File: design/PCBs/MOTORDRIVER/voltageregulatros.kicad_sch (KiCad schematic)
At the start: 15 parts, among them IC2 LD1117S33CTR, IC3 MC34063ECD-TR, IC4 BQ24133RGYR, IC5 REF3450TIDBVR

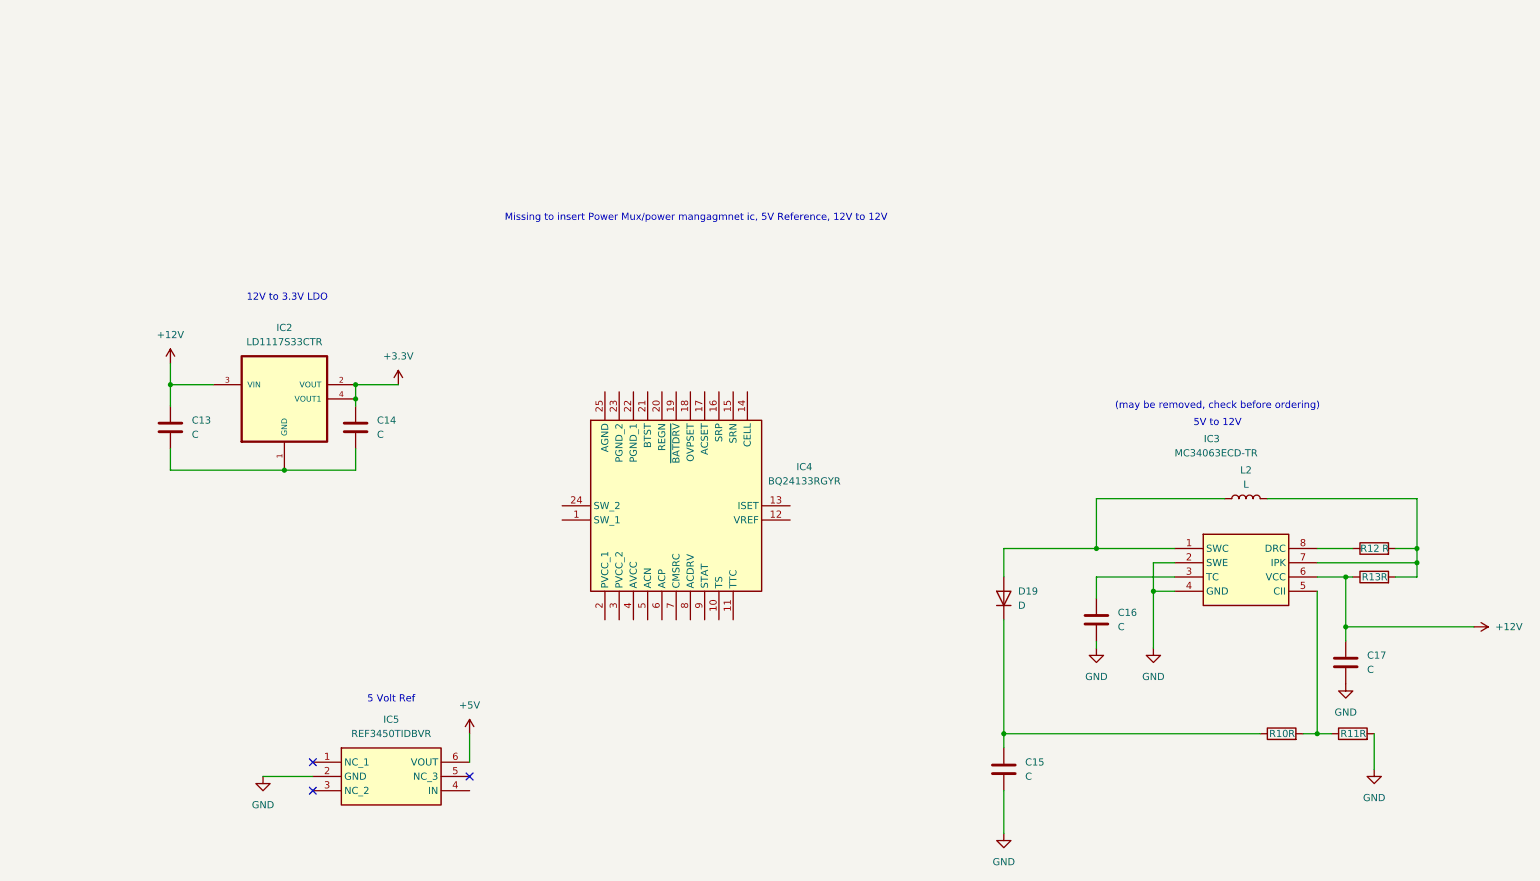
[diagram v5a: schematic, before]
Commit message: Clearer file names for datasheets indicating what kind of component they are. Started on connecting the battery charger Added mosfet ICs for driver gates
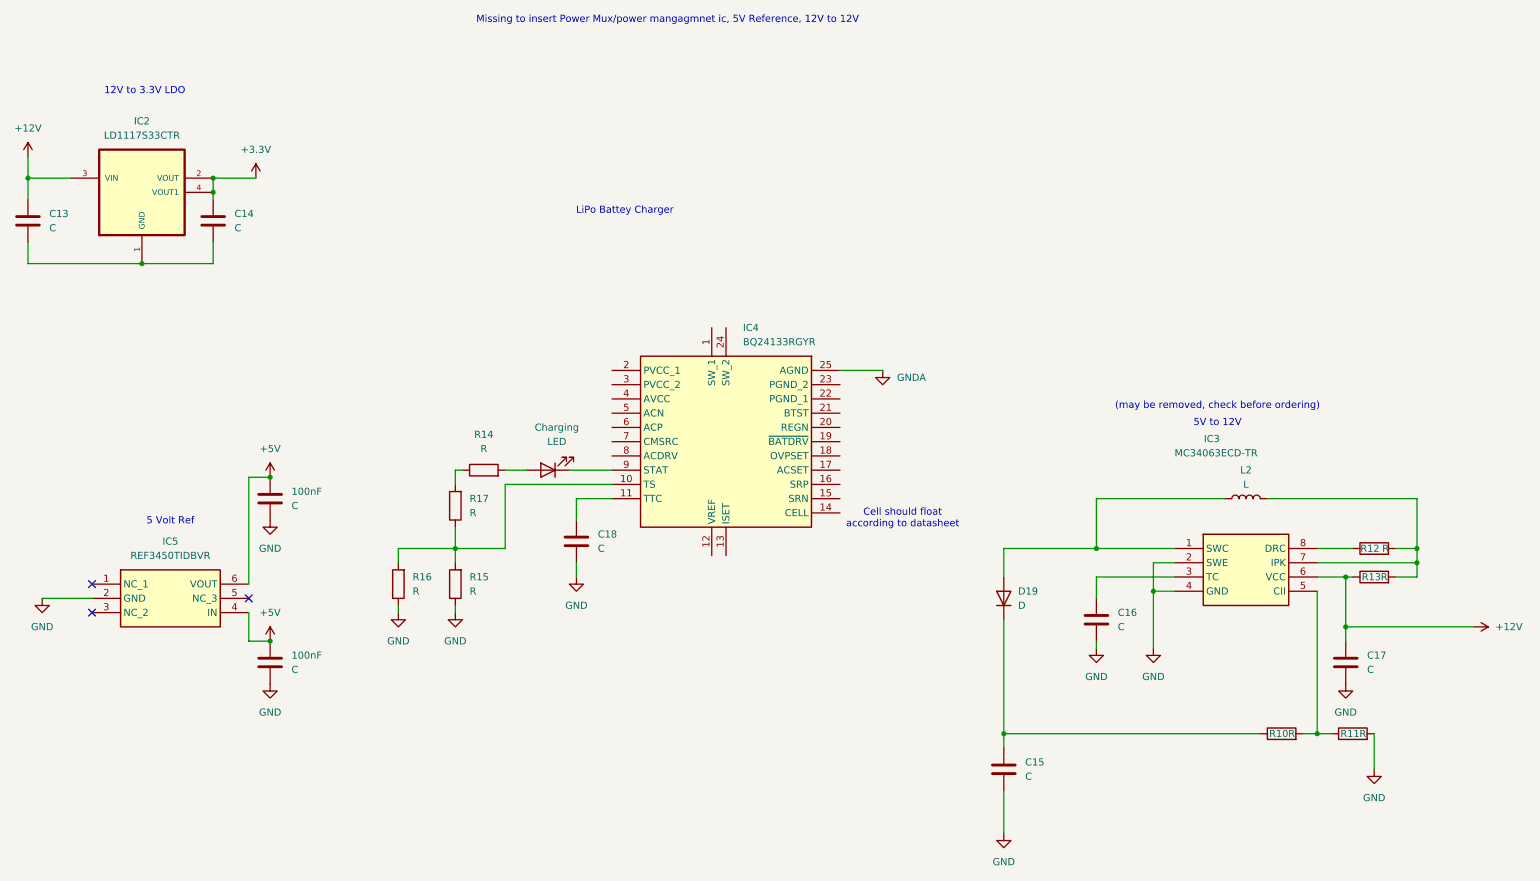
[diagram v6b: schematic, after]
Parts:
- added 100nF (x2), C18: C, symbol Device:C
- added Charging: LED, symbol Device:LED
- added R14, R15, R16, R17: R, symbol Device:R
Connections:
- net +5V: now also IC5.4 (IN), 100nF.1, 100nF.1
- net GND: now also 100nF.2, 100nF.2, C18.2, R15.1, R16.1
- net at IC4.10 (TS): now also R15.2, R16.2, R17.1
- net at IC4.11 (TTC): now also C18.1
- net GNDA: now reaches IC4.25 (AGND)
- net at IC4.9 (STAT): now also Charging.1 (K)
- new net: R14.1, R17.2
- new net: Charging.2 (A), R14.2
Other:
- note added: "Cell should float according to datasheet"
- note added: "LiPo Battey Charger"
- moved on the sheet: C13, C14, IC2, IC4, IC5

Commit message: fixed schematic layout and added shunt resistor and zener diodes for motor stage
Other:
- note added: "12V out"
- note removed: "(may be removed, check before ordering)"
- note removed: "5V to 12V"
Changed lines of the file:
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@@
-		)
-	)
-	(text "(may be removed, check before ordering)\n"
-		(exclude_from_sim no)
-		(at 234.95 76.2 0)
-		(effects
-			(font
-				(size 1.27 1.27)
-			)
 		)
 	)
@@
 		)
 	)
-	(text "5V to 12V"
+	(text "12V out"
 		(exclude_from_sim no)
 		(at 234.95 79.248 0)
@@
 	(text "LiPo Battey Charger\n"
 		(exclude_from_sim no)
-		(at 129.286 41.402 0)
+		(at 145.542 57.658 0)
 		(effects
 			(font

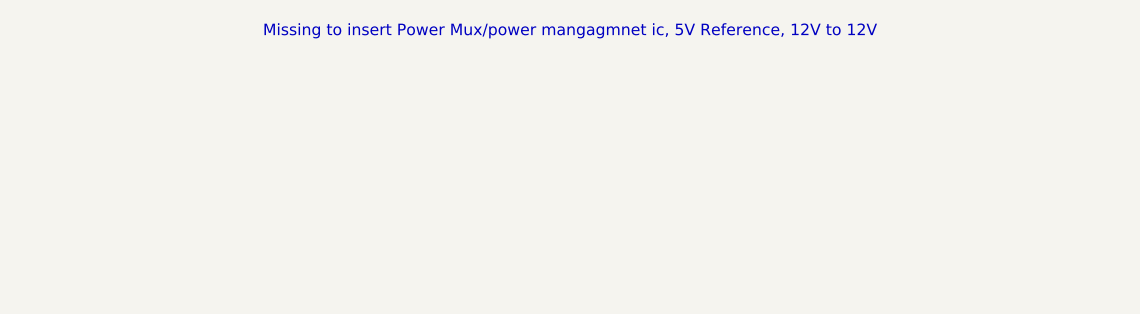
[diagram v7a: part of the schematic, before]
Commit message: added lables and worked on the motor stage, changed the mosfet driver
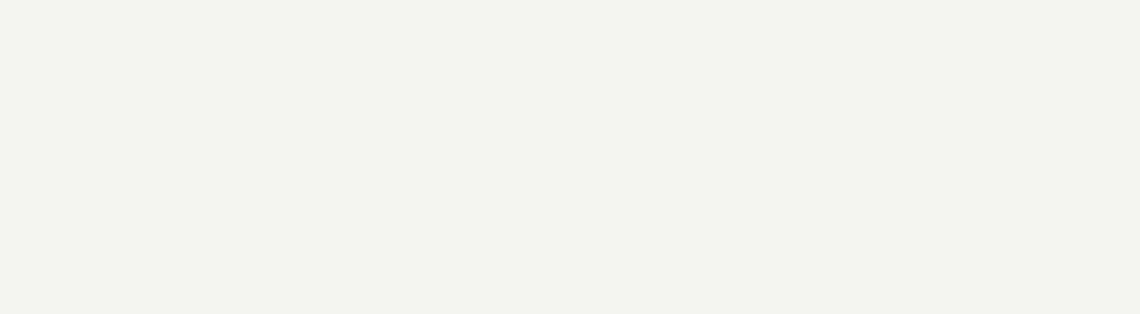
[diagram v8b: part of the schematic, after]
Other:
- note removed: "Missing to insert Power Mux/power mangagmnet ic, 5V Reference, 12V to 12V"
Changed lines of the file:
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@@
-		)
-	)
-	(text "Missing to insert Power Mux/power mangagmnet ic, 5V Reference, 12V to 12V"
-		(exclude_from_sim no)
-		(at 136.906 7.366 0)
-		(effects
-			(font
-				(size 1.27 1.27)
-			)
 		)
 	)
